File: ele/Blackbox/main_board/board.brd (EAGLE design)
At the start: 111.7 x 112.7 mm, 183 parts, among them IC1 DS3231/SO, IC2 QMC5883L-TR, Q2 BSO201SP, Q8 BSO201SP, Q9 BSO201SP, U1 MPU-6050

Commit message: 2.KSK
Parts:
- removed Q4: (no value), transistors:SOT23
- removed R21: 100k, rcl:R0603
- removed R23, R24: 10k, rcl:R0402
- added C71: 4.7uf, rcl:C0603
- R18: value 10k -> 2M; device rcl:R0402 -> rcl:R0603
- moved R18 11.7 mm to (-2.54, -24.1), turned to 90 degrees
- moved C5 10.1 mm to (-3.81, 19.1), turned to 180 degrees
- moved C2 9.92 mm to (-0.52, 27.8), turned to 90 degrees
- moved C4 9.09 mm to (1.27, 19.1), turned to 0 degrees
- moved C3 6.79 mm to (2.03, 22.9), turned to 90 degrees
- moved R19 5.08 mm to (19.1, -1.27)
- moved U1 1.27 mm to (-1.27, 22.9), turned to 0 degrees
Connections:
- removed net N$7: IC1.1, R21.1
- removed net TX_485-5V: MAX1.4, Q4.3, R24.2
- new net IO10_NC4: U1.22
- new net IO9_NC4: U1.19
- new net IO9_NC5: U1.21
- net +3V3: no longer Q4.1, R21.2, R23.1
- net +5V: no longer R18.2, R24.1
- net ESP_SHUTDOWN: now also IM1.25; no longer IM1.33
- net N$6: now also C71.1, R18.1
- net RX-485-5V: no longer R18.1
- net SQW/INT: now also IM1.33; no longer IM1.25
- net SW0: now also C71.2, R18.2
- net TX_485: now also MAX1.4; no longer Q4.2, R23.2
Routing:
- net TX_485-5V: track 59.4 -> 0.00 mm
- net TX_485: track 19.6 -> 74.5 mm
- net SW0: track 23.4 -> 59.0 mm, vias 0 -> 2
- net +3V3: track 208.9 -> 233.0 mm, vias 5 -> 6
- net +5V: track 112.3 -> 96.8 mm
- net SQW/INT: track 67.9 -> 54.6 mm, vias 1 -> 2
- net ESP_SHUTDOWN: track 51.4 -> 39.5 mm
- net N$6: track 6.74 -> 13.6 mm
- net RX-485-5V: track 62.0 -> 56.5 mm
- net INT_MPU5060: track 49.4 -> 44.5 mm, vias 2 -> 0
- net N$7: track 4.01 -> 0.00 mm
- net SDA: track 93.2 -> 90.9 mm, vias 2 -> 3
- net SCL: track 90.4 -> 91.3 mm
- net N$3: track 2.67 -> 3.21 mm
- net GND: vias 129 -> 131

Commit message: dovetek_2.KSK
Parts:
- moved R13 79.5 mm to (39.8, 22.2)
- moved Q1 79.5 mm to (86.4, 52.1)
- moved Q10 79.5 mm to (82.5, 52.1)
- moved R11 79.3 mm to (74.9, 29.6)
- moved R12 79.3 mm to (37.5, 22.2)
- moved R10 79.2 mm to (72.4, 30.5), turned to 180 degrees
- moved X2 79.2 mm to (55.9, 11.7)
- moved Q8 79.2 mm to (53.5, 18.5)
- moved Q9 79.2 mm to (50.3, 26.8)
- moved C12 79.2 mm to (100.7, 70.5)
- moved C13 79.2 mm to (98.9, 75.1)
- moved C14 79.2 mm to (96.7, 79.5)
- moved C16 79.2 mm to (90.9, 87.4)
- moved C17 79.2 mm to (87.4, 90.9)
- moved C2 79.2 mm to (55.5, 83.8)
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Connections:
- net MODE_485: now also IM1.15; no longer IM1.24
- net MOTOR: now also IM1.24; no longer IM1.15
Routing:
- net MODE_485: track 47.2 -> 73.9 mm, vias 0 -> 1
- net MOTOR: track 28.6 -> 17.1 mm
- net VCC: track 257.4 -> 268.1 mm
- net ESP_SHUTDOWN: track 39.5 -> 35.0 mm
- net +3V3: track 233.0 -> 228.5 mm
- net N$71: track 16.5 -> 13.7 mm
- net +5V: track 96.8 -> 94.9 mm
- net RX-485-5V: track 56.5 -> 55.4 mm
- net WS2812-5V: track 36.0 -> 37.0 mm
- net N$62: track 8.05 -> 7.22 mm
- net RX_485: track 16.4 -> 15.7 mm
- net WS2812: track 13.3 -> 12.5 mm
- net GND: vias 131 -> 133
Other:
- board size 111.7 x 112.7 mm -> 112.7 x 112.7 mm

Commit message: 3.KSK
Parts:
- added Q4: BSS84, Transistor:SOT23
- added R21, R23, R26: 180, rcl:R0402
- moved R1 27.6 mm to (52.1, 41.9)
- moved R10 2.55 mm to (74.9, 30.7), turned to 0 degrees
- moved R4 1.40 mm to (74.9, 57.1)
- moved R11 0.38 mm to (74.9, 29.2)
- moved R19 0.17 mm to (74.9, 54.6)
- moved R5 0.17 mm to (74.9, 55.9)
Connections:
- new net !ENC-A: R23.1, U$62.A
- new net !ENC-B: R21.1, U$62.B
- new net !SW0: C71.2, Q4.1, R1.1, R18.2, U$62.P$4
- new net SW!0: Q4.3, R26.1
- net +3V3: now also Q4.2
- net ENC-A: now also IM1.29, R23.2; no longer IM1.30, U$62.A
- net ENC-B: now also R21.2; no longer U$62.B
- net MOTOR: now also IM1.10; no longer IM1.24
- net SW0: now also IM1.30, R26.2; no longer C71.2, IM1.29, R1.1, R18.2, U$62.P$4
- net TX_485: now also IM1.24; no longer IM1.10
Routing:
- net SW0: track 59.1 -> 2.04 mm, vias 2 -> 0
- net !SW0: track 0.00 -> 40.6 mm, vias 0 -> 2
- net +3V3: track 228.5 -> 262.8 mm, vias 6 -> 7
- net TX_485: track 74.0 -> 40.2 mm
- net SW!0: track 0.00 -> 26.6 mm
- net MOTOR: track 17.1 -> 38.8 mm, vias 1 -> 0
- net ENC-A: track 28.6 -> 10.8 mm
- net !ENC-A: track 0.00 -> 13.5 mm
- net ENC-B: track 19.3 -> 10.2 mm
- net !ENC-B: track 0.00 -> 7.94 mm
- net ESP_SHUTDOWN: track 35.0 -> 36.5 mm
- net WS2812-5V: track 37.0 -> 36.2 mm

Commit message: ladeni_drah
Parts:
- removed R1: 10k, rcl:R0402
- added D2: (no value), diode:DO214BA
- added R24: 10k, rcl:R0402
- C6: device rcl:C0402K -> rcl:C0603
- C7: device rcl:C0603 -> rcl:C0402
- R26: value 180 -> 220
- moved JP3 53.5 mm to (81.3, 45.7), turned to 0 degrees
- moved R2 25.9 mm to (69.8, 77.5), turned to 0 degrees
- moved R3 24.7 mm to (58.4, 69.8), turned to 270 degrees
- moved C7 4.48 mm to (62.0, 93.1), turned to 0 degrees
- moved JP4 3.81 mm to (31.8, 68.6)
- moved C6 2.16 mm to (59.2, 93.1), turned to 270 degrees
- moved C8 1.78 mm to (52.1, 93.2), turned to 180 degrees
- moved C1 1.42 mm to (26.7, 74.3)
- moved IC2 1.27 mm to (55.9, 94.0)
- moved R13 0.57 mm to (40.0, 21.7)
- moved R12 0.51 mm to (37.5, 21.7)
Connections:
- removed net AD0: U1.9
- removed net CLKIN: U1.1
- removed net FSYNC: U1.11
- net !SW0: no longer R1.1
- net +3V3: no longer R1.2
- net GND: now also D2.A, R24.2, U1.1, U1.11, U1.9
- net RX-GPS: now also IM1.27; no longer IM1.26
- net SW0: now also R24.1
- net TX-GPS: now also IM1.26; no longer IM1.27
- net VCC: now also D2.C
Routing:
- net TX-GPS: track 43.9 -> 14.3 mm
- net RX-GPS: track 46.5 -> 17.9 mm
- net N$4: track 53.7 -> 35.9 mm
- net SDA: track 90.9 -> 98.5 mm
- net +3V3: track 262.8 -> 256.5 mm, vias 7 -> 8
- net SCL: track 91.1 -> 95.5 mm
- net QMC5883-INTERRUPT: track 40.8 -> 45.0 mm
- net N$62: track 7.22 -> 4.11 mm
- net VCC: track 268.1 -> 265.5 mm
- net N$66: track 2.26 -> 4.31 mm
- net SW0: track 2.04 -> 4.08 mm
- net SW!0: track 26.6 -> 28.6 mm
- net GND: track 1.47 -> 3.04 mm, vias 133 -> 138
- net N$60: track 1.18 -> 2.61 mm
- net DS3231/RST: track 65.5 -> 64.3 mm
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
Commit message: ladeni_drah
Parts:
- added C72, C73, C74: 10uf, rcl_upravena:C0402
- added JP5: (no value), pinhead:1X04
- C1, C10, C11, C12, C13, C14, C15, C16, C17, C18, C19, C2, C20, C21, C22, C23, C24, C25, C26, C27, C28, C29, C3, C30, C31, C32, C33, C34, C35, C36, C37, C38, C39, C40, C42, C43, C44, C45, C46, C47, C48, C49, C5, C50, C51, C52, C53, C54, C55, C56, C57, C58, C59, C60, C61, C62, C63, C64, C65, C66, C67, C68, C9: device rcl:C0402K -> rcl_upravena:C0402
- C41: value (none) -> 100pf; device rcl:C0402K -> rcl_upravena:C0402
- C6: device rcl:C0603 -> rcl_upravena:C0402
- C7: device rcl:C0402 -> rcl_upravena:C0402
- C71: device rcl:C0603 -> rcl_upravena:C0603
- C8: device rcl:C0402K -> rcl_upravena:C0402P
- R18: value 2M -> 1M
- R24: value 10k -> 47k
- U$1: value CR2032THM -> CR2032; device CR2032:CR2032-THRU -> CR2032:CH075
- moved C7 7.03 mm to (56.6, 97.7)
- moved C8 6.76 mm to (58.2, 96.0), turned to 90 degrees
- moved C6 6.37 mm to (56.6, 98.9), turned to 0 degrees
- moved Q4 4.95 mm to (50.9, 44.5), turned to 90 degrees
- moved R20 3.96 mm to (25.2, 77.5), turned to 270 degrees
- moved U$1 2.84 mm to (25.4, 81.3)
- moved C4 2.32 mm to (54.9, 74.5), turned to 270 degrees
- moved IC2 1.27 mm to (55.9, 95.2), turned to 90 degrees
- moved R3 1.27 mm to (58.4, 68.6)
- moved C5 0.73 mm to (52.6, 75.4)
- moved C2 0.65 mm to (55.4, 83.2)
- moved R24 0.51 mm to (69.3, 59.7)
- moved C3 0.27 mm to (57.8, 78.7)
- moved R10 0.25 mm to (74.9, 30.5)
- moved Q5 0.12 mm to (56.0, 31.8)
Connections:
- net IO10_NC3 renamed IO9_NC6
- removed net IO11_NC2: IC2.6
- removed net SW!0: Q4.3, R26.1
- new net IO9_NC7: IC2.7
- new net N$7: Q4.2, R26.1
- net +3V3: now also C72.1, C73.1, C74.1, JP5.4, R24.2; no longer Q4.2
- net 3,3!KNOFLIK: now also U$1.+; no longer U$1.+1, U$1.+2
- net GND: now also C72.2, C73.2, C74.2, JP5.3, Q4.3; no longer R24.2
- net IO10_NC2: now also IC2.6; no longer IC2.5
- net IO9_NC2: now also IC2.5; no longer IC2.14
- net IO9_NC3: now also IC2.14; no longer IC2.7
- net SCL: now also JP5.2
- net SDA: now also JP5.1
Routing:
- net SW!0: track 28.6 -> 0.00 mm
- net N$7: track 0.00 -> 21.8 mm
- net 3,3!KNOFLIK: track 27.7 -> 9.05 mm
- net +3V3: track 256.5 -> 251.1 mm
- net SCL: track 95.5 -> 99.9 mm
- net N$66: track 4.31 -> 1.02 mm
- net !SW0: track 39.6 -> 36.6 mm
- net QMC5883-INTERRUPT: track 45.0 -> 42.7 mm
- net SDA: track 98.5 -> 100.2 mm
- net N$62: track 4.11 -> 5.74 mm
- net GND: track 3.04 -> 1.47 mm, vias 138 -> 152
- net N$3: track 3.07 -> 1.62 mm
- net N$9: track 19.2 -> 18.4 mm
- net TX-GPS: track 14.3 -> 15.0 mm
- net RX-GPS: track 17.9 -> 18.6 mm
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- removed copper zone on layer 1, net +3V3
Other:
- board text added: "!+5V"
- board text added: "+5V"
- board text added: "+5v"
- board text added: "A"
- board text added: "B"
- board text added: "GND"
- board text added: "RB3203_BLACK-BOX-BOARD_V1"

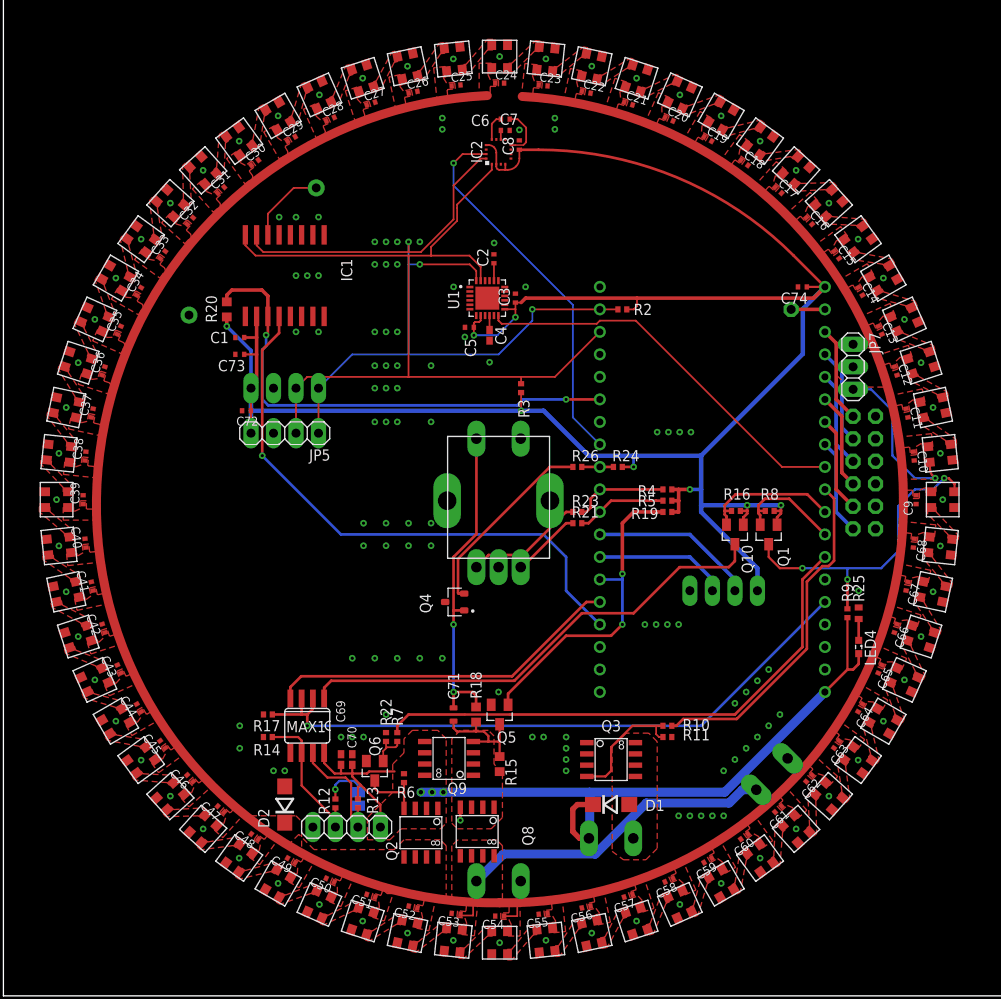
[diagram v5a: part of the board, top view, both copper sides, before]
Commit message: jina_poloha_MPU6050
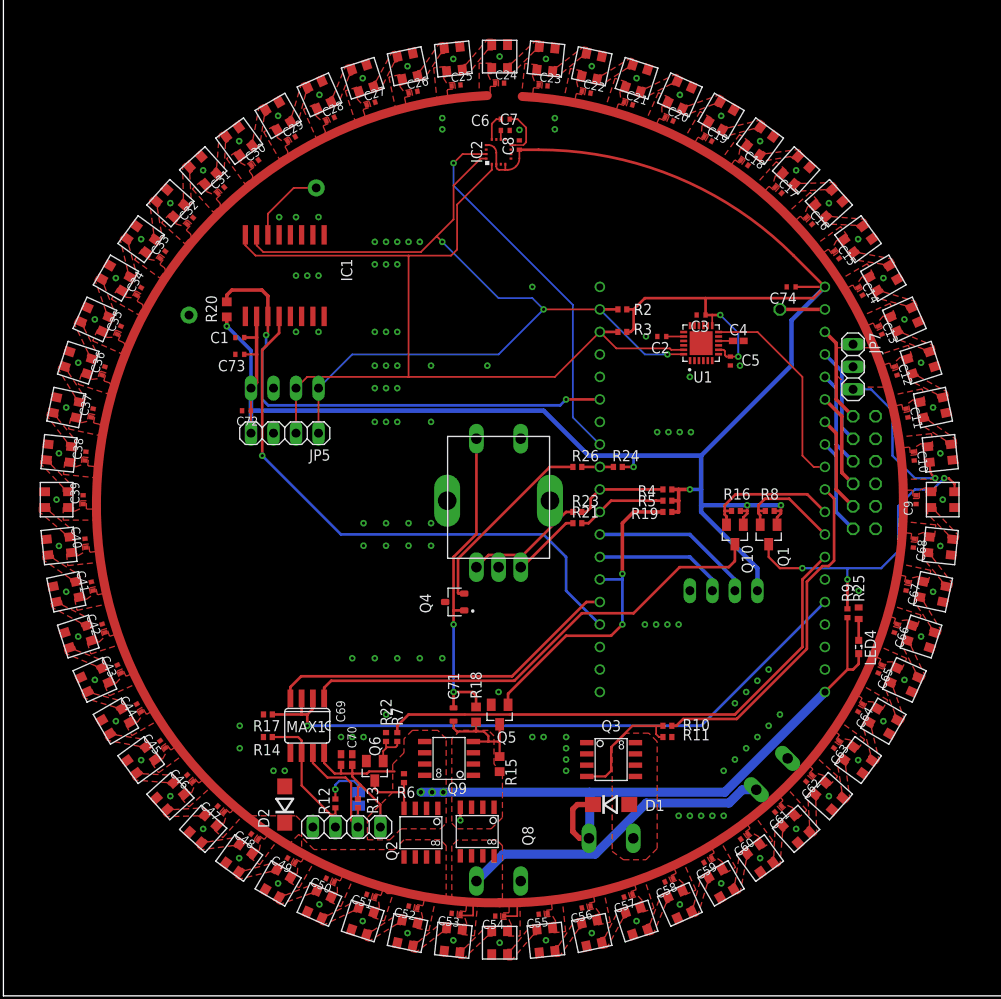
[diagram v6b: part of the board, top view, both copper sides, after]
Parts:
- moved C5 29.7 mm to (82.0, 71.6), turned to 270 degrees
- moved C4 28.1 mm to (82.9, 73.9), turned to 0 degrees
- moved U1 24.7 mm to (78.7, 73.7), turned to 90 degrees
- moved C3 21.0 mm to (78.7, 76.8), turned to 180 degrees
- moved C2 20.9 mm to (74.3, 74.4), turned to 180 degrees
- moved R3 13.1 mm to (69.8, 74.9), turned to 0 degrees
- moved JP8 1.27 mm to (87.6, 77.5)
- moved C74 1.27 mm to (88.9, 80.0)
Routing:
- net INT_MPU5060: track 44.5 -> 23.5 mm
- net +3V3: track 251.1 -> 240.9 mm, vias 8 -> 7
- net SCL: track 99.9 -> 105.1 mm
- net SDA: track 100.2 -> 103.6 mm
- net N$10: track 3.81 -> 5.08 mm
- net GND: vias 152 -> 153

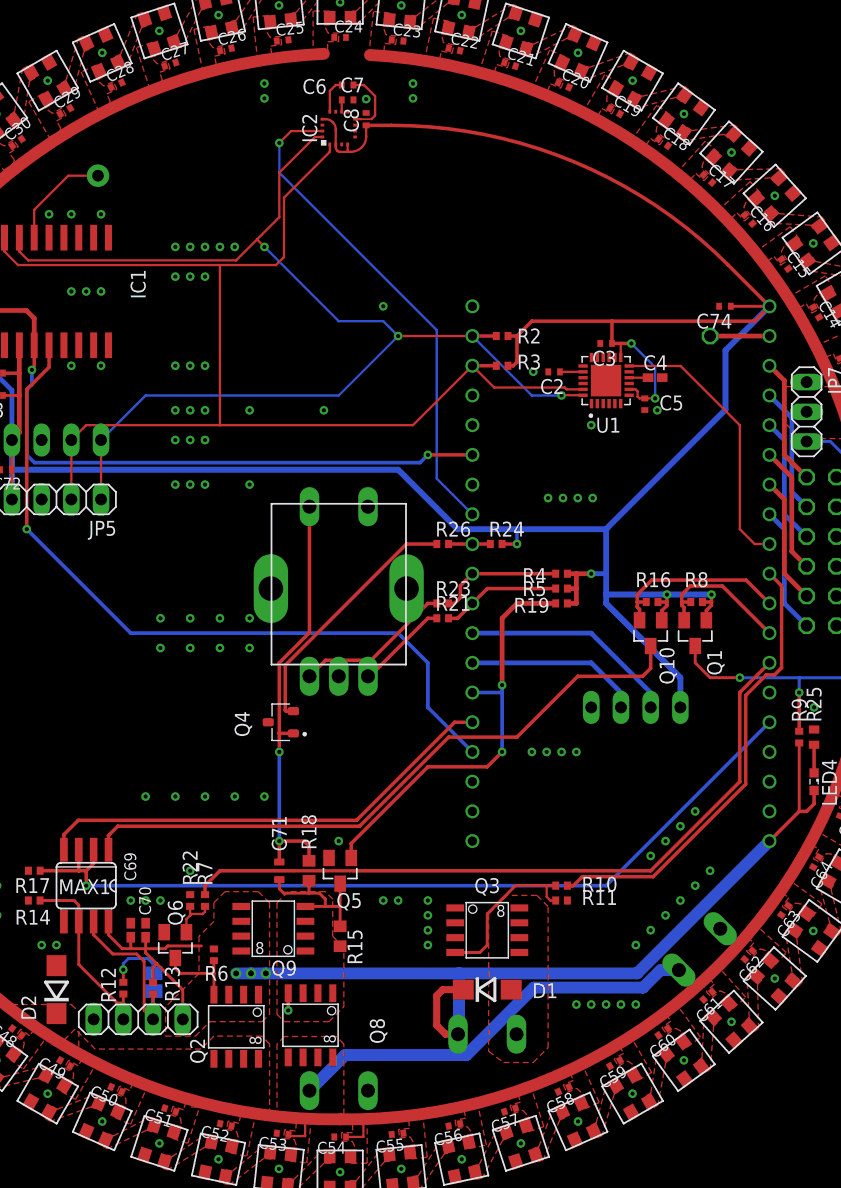
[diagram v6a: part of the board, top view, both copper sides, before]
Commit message: srazeni_ceny
-vymena_tranzistoru
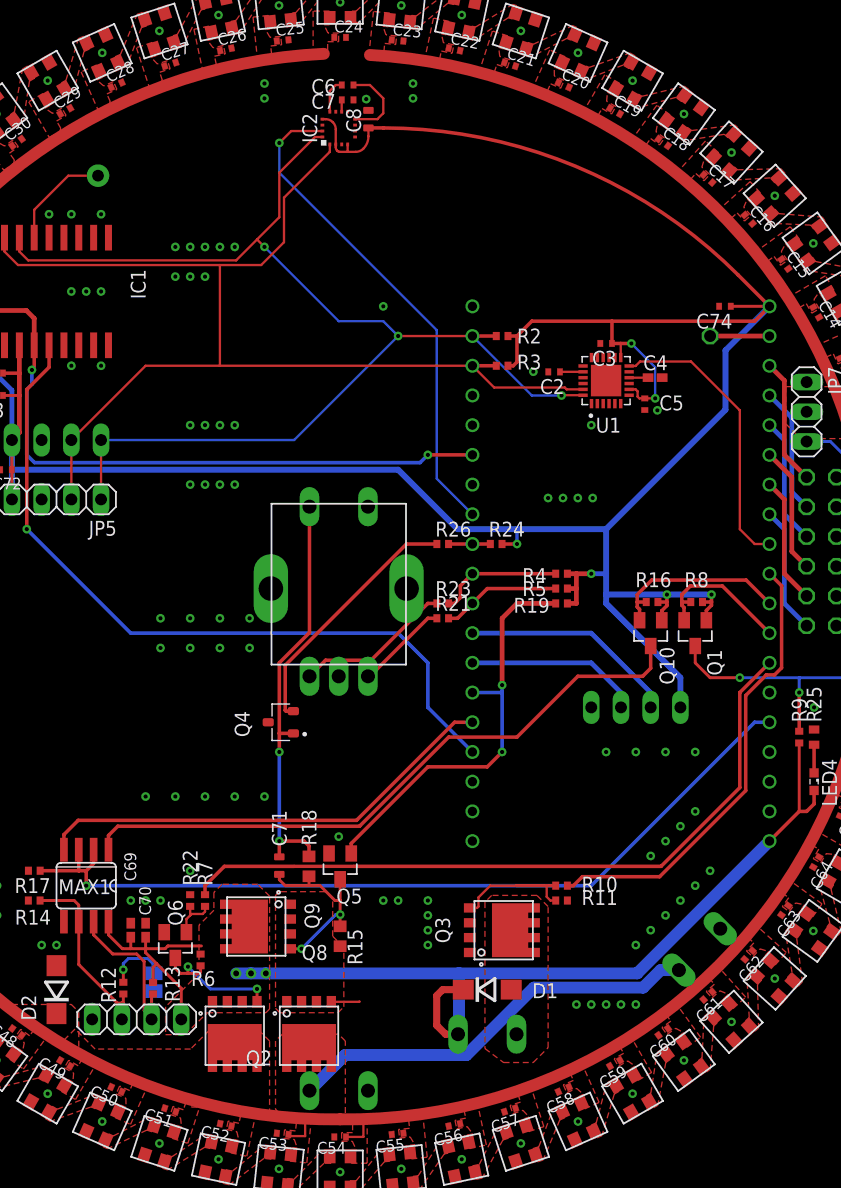
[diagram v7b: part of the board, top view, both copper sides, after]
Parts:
- C8: device rcl_upravena:C0402P -> rcl_upravena:C0603
- Q2, Q8, Q9: value BSO201SP -> AO3401ASOP-8_EP_5.0X5.0X1.27P; device transistor-fet:SO-8 -> transistor-fet:SOP-8_EP_5.0X5.0X1.27P
- Q3: value (none) -> AO3401ASOP-8_EP_5.0X5.0X1.27P; device transistors:SO-8 -> transistor-fet:SOP-8_EP_5.0X5.0X1.27P
- moved R6 1.22 mm to (44.1, 24.1)
- moved Q2 0.65 mm to (47.0, 19.1), turned to 0 degrees
- moved Q8 0.52 mm to (53.3, 19.1), turned to 0 degrees
- moved C71 0.44 mm to (50.8, 32.2)
- moved Q5 0.38 mm to (56.0, 32.1)
- moved R18 0.38 mm to (53.3, 32.1)
- moved Q9 0.20 mm to (50.2, 27.0), turned to 270 degrees
- moved C8 0.19 mm to (58.4, 96.0)
- moved JP1 0.13 mm to (38.6, 19.1)
- turned Q3 to 90 degrees
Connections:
- net +5V: now also Q9.9
- net N$2: now also Q3.9
- net N$4: now also Q8.9
- net VCC: now also Q2.9
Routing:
- net SCL: track 105.1 -> 99.3 mm
- net N$68: track 7.27 -> 12.2 mm, vias 0 -> 2
- net N$71: track 14.4 -> 10.5 mm
- net N$6: track 13.6 -> 16.7 mm, vias 0 -> 2
- net N$62: track 5.74 -> 6.91 mm
- net INT_MPU5060: track 23.5 -> 24.6 mm
- net GND: track 1.47 -> 2.42 mm, vias 153 -> 145
- net !SW0: track 36.6 -> 35.8 mm

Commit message: diry_pro_srouby
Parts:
- C8: device rcl_upravena:C0603 -> rcl_upravena:C0402P
- R2, R3: value 47k -> 10k
- R20: device rcl:R0603 -> rcl:R0402
- R25: value 1k -> 270
- moved R13 0.14 mm to (39.9, 21.7)
- moved R12 0.13 mm to (37.3, 21.7)
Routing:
- net +3V3: track 240.5 -> 241.1 mm
